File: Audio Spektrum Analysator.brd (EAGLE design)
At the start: 144.8 x 98.7 mm, 148 parts, among them IC1 LM324N, IC10 LM3914N, IC11 LM3914N, IC12 LM3914N, IC13 LM3914N, IC2 LM324N, IC3 LM324N, IC4 LM3914N, IC5 LM3914N, IC6 LM3914N, IC7 LM3914N, IC8 LM3914N, IC9 LM3914N, J2 DCJ0202, M1 ELECTRET_MICROPHON-F6050AP

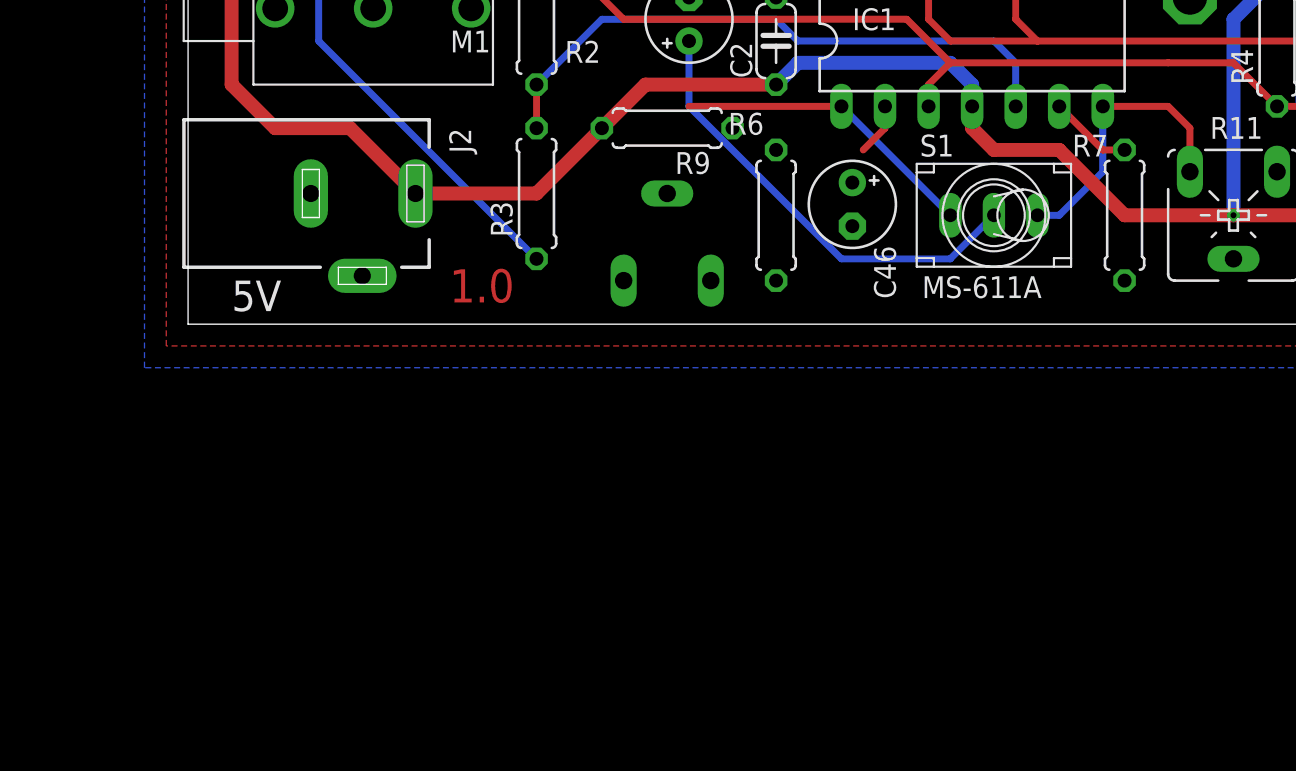
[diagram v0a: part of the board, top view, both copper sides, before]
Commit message: edited preamp
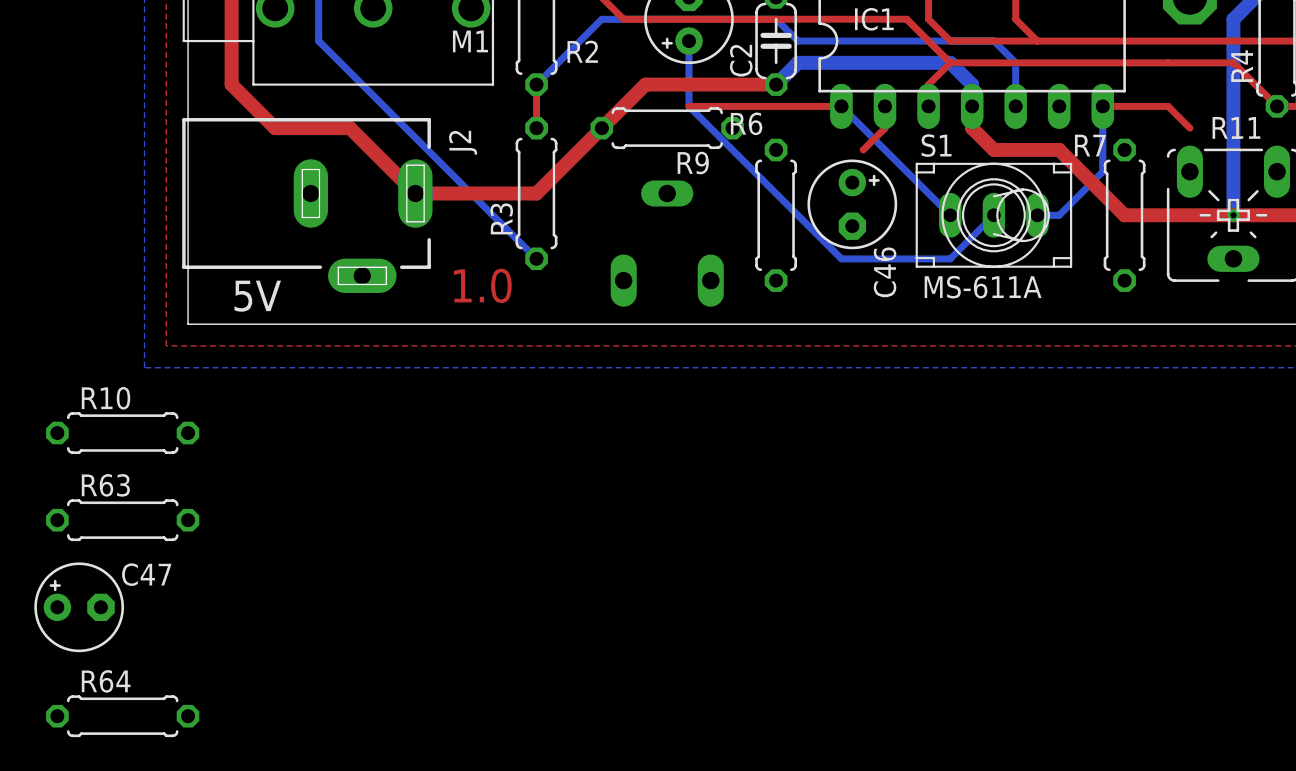
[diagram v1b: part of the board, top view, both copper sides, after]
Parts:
- added C47: 2u2, resistor:E2,5-5
- added R10, R63: 47k, rcl:0207/7
- added R64: 10k, rcl:0207/7
- R7: value 10k -> 100k
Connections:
- removed net N$123: IC1.6, R11.S, R7.2
- new net N$57: C47.+, IC1.6, R7.1
- new net N$70: C47.-, R64.2
- new net N$83: R11.E, R64.1
- net +5V: now also R63.2
- net GND: now also R10.1, R11.S; no longer R7.1
- net N$10: now also R7.2; no longer R11.E
- net N$3: now also R10.2, R63.1
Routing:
- net N$123: track 4.86 -> 0.00 mm
- net N$10: track 16.8 -> 14.3 mm

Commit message: edited reference circuit of LM3916s
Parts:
- removed R45: 1k2, resistor:0207/7
- removed R48, R50, R52, R54, R56, R58, R60, R62: 7k5, resistor:0207/7
- added R65: 1M, rcl:0207/7
- added R66, R67: 100k, rcl:0207/7
- added R68: 1k2, resistor:0207/7
- R43: value 1k2 -> 20k
- R44: value 7k5 -> 20k
- R46: value 7k5 -> 1k2
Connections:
- removed net N$107: IC4.6, IC4.7, R43.2
- removed net N$120: IC11.6, IC11.7, R57.2
- removed net N$121: IC11.8, R57.1, R58.2
- removed net N$127: IC12.6, IC12.7, R59.2
- removed net N$128: IC12.8, R59.1, R60.2
- removed net N$179: IC13.6, IC13.7, R61.2
- removed net N$180: IC13.8, R61.1, R62.2
- removed net N$82: IC10.8, R55.1, R56.2
- removed net N$94: IC9.6, IC9.7, R53.2
- removed net N$95: IC9.8, R53.1, R54.2
- new net RHI: IC10.6, IC11.6, IC12.6, IC13.6, IC4.6, IC5.6, IC6.6, IC7.6, IC8.6, IC9.6, R43.1, R44.2
- net +5V: now also R43.2
- net GND: now also IC10.8, IC11.8, IC12.8, IC13.8, IC4.8, IC5.8, IC6.8, IC7.8, IC8.8, IC9.8, R47.1, R49.1, R51.1, R53.1, R55.1, R57.1, R59.1, R61.1, R65.1, R66.1, R67.1, R68.1; no longer R48.1, R50.1, R52.1, R54.1, R56.1, R58.1, R60.1, R62.1
- net N$108: now also IC4.7, R68.2; no longer IC4.8, R43.1, R44.2
- net N$29: no longer IC6.6
- net N$30: now also IC5.7, R46.2; no longer IC6.8, R47.1, R48.2
- net N$42: now also IC7.7, R49.2; no longer IC5.6, IC5.7, R45.2
- net N$43: now also IC8.7, R51.2; no longer IC5.8, R45.1, R46.2
- net N$55: now also IC10.7, R55.2; no longer IC7.6, IC7.7, R49.2
- net N$56: now also IC9.7, R53.2; no longer IC7.8, R49.1, R50.2
- net N$68: now also IC11.7, R57.2; no longer IC8.6, IC8.7, R51.2
- net N$69: now also IC12.7, R59.2; no longer IC8.8, R51.1, R52.2
- net N$81: now also IC13.7, R61.2; no longer IC10.6, IC10.7, R55.2
- net OUT1: now also R66.2
- net OUT2: now also R67.2
- net VER: now also R65.2
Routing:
- net RHI: track 0.00 -> 39.9 mm
- net N$95: track 14.4 -> 0.00 mm
- net N$82: track 14.4 -> 0.00 mm
- net N$69: track 14.4 -> 0.00 mm
- net N$128: track 14.4 -> 0.00 mm
- net N$121: track 14.4 -> 0.00 mm
- net N$56: track 14.4 -> 0.00 mm
- net N$30: track 14.4 -> 0.00 mm
- net N$108: track 14.4 -> 0.00 mm
- net N$180: track 14.4 -> 0.00 mm
- net N$43: track 14.4 -> 0.00 mm
- net N$127: track 6.77 -> 0.00 mm
- net N$120: track 6.77 -> 0.00 mm
- net N$107: track 6.77 -> 0.00 mm
- net N$55: track 6.77 -> 0.00 mm
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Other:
- board text added: "DC IN"
- board text removed: "5V"

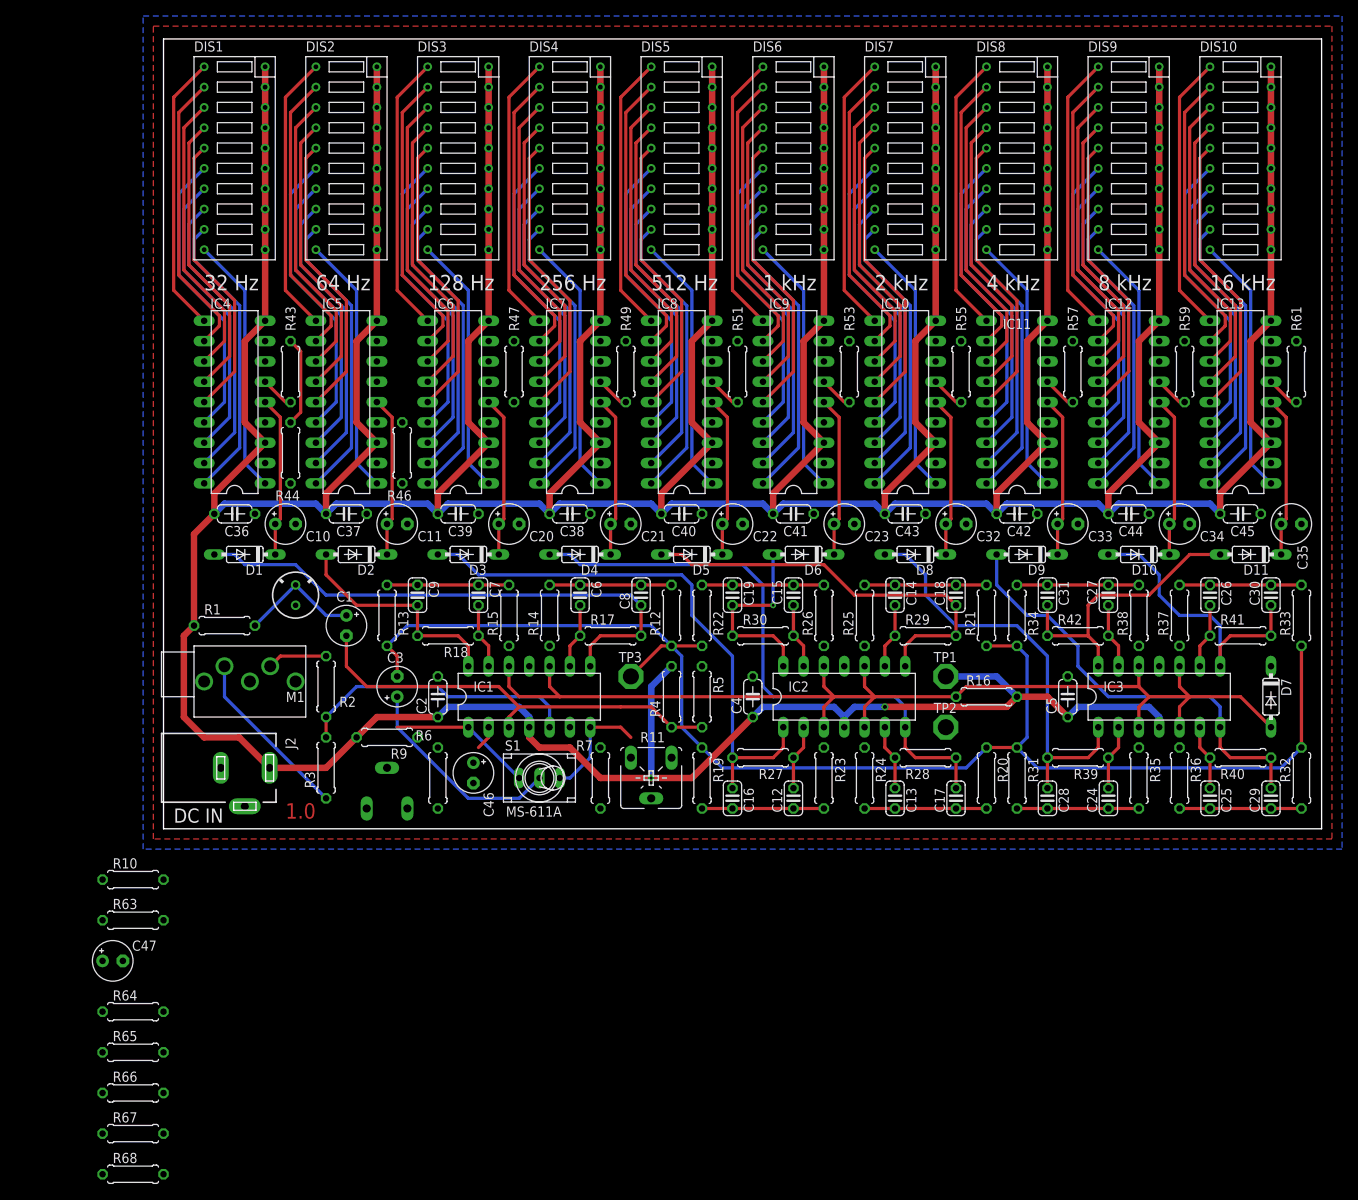
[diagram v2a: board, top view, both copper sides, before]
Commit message: started connecting Lm3916s
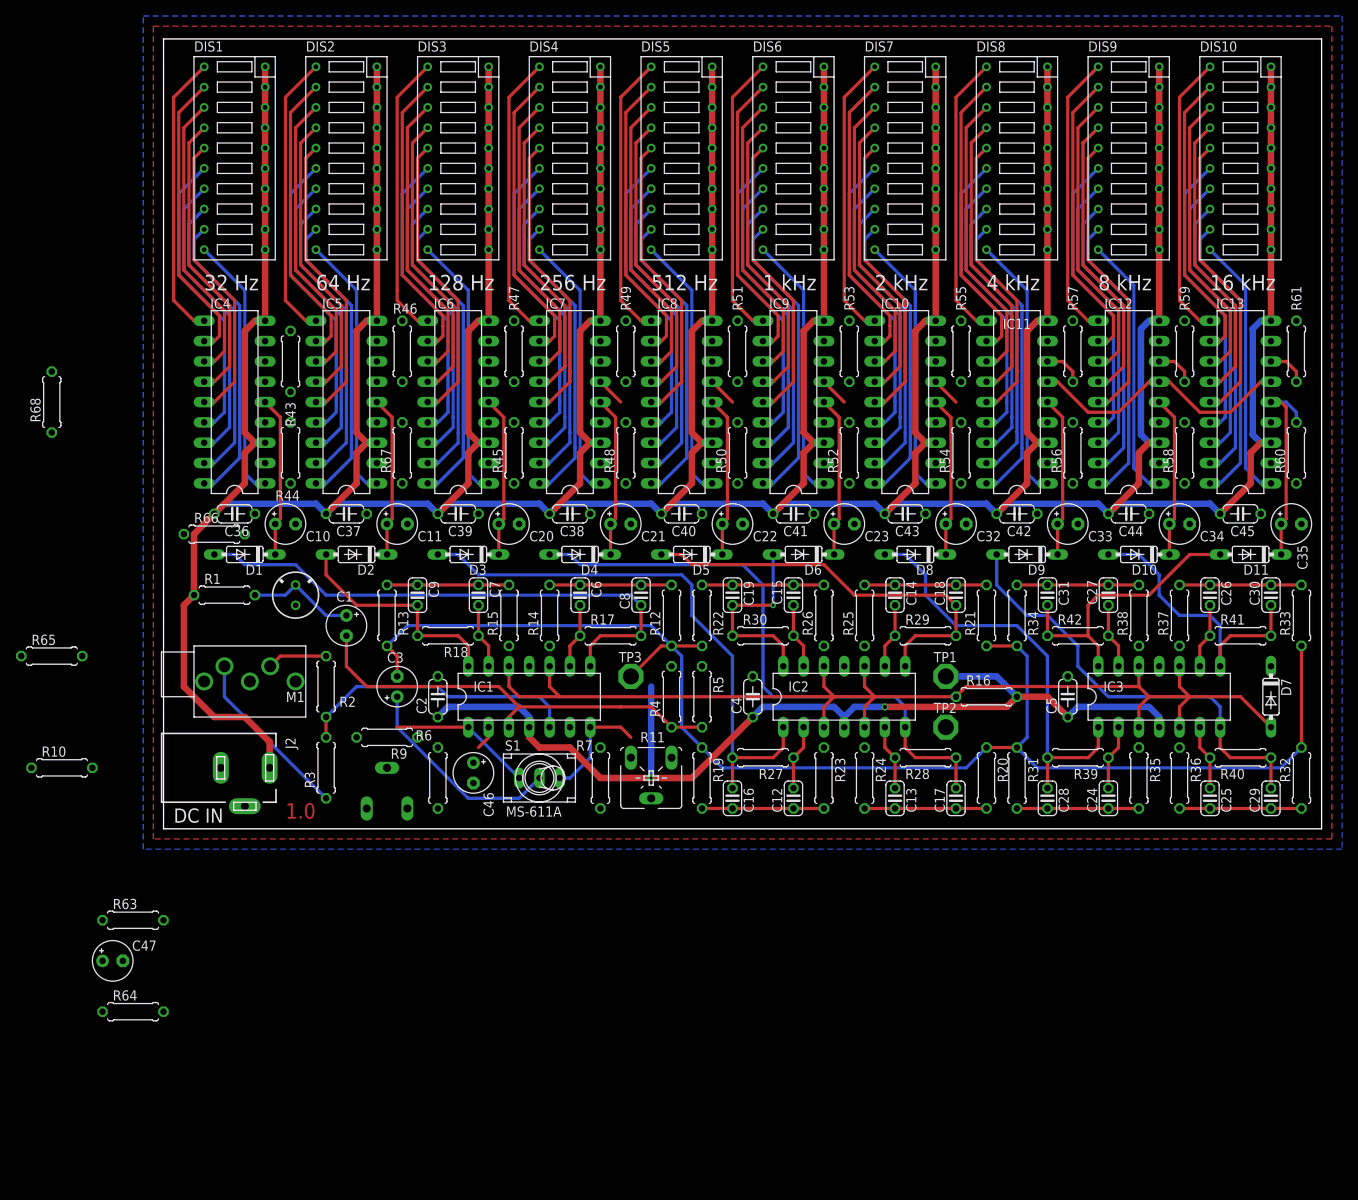
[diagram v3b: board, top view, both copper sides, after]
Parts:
- added R45, R48, R50, R52, R54, R56, R58, R60: 100k, rcl:0207/7
- moved R68 97.1 mm to (-14.0, 53.3), turned to 90 degrees
- moved R67 91.5 mm to (29.8, 47.0), turned to 90 degrees
- moved R66 70.6 mm to (6.35, 36.8)
- moved R65 50.6 mm to (-14.0, 21.6)
- moved R10 16.6 mm to (-12.7, 7.62)
- moved R46 12.7 mm to (29.8, 59.7), turned to 270 degrees
- moved R1 3.81 mm to (7.62, 29.2)
- moved R47 2.54 mm to (43.8, 59.7)
- moved R49 2.54 mm to (57.8, 59.7)
- moved R51 2.54 mm to (71.8, 59.7)
- moved R53 2.54 mm to (85.7, 59.7)
- moved R55 2.54 mm to (99.7, 59.7)
- moved R57 2.54 mm to (113.7, 59.7)
- moved R59 2.54 mm to (127.6, 59.7)
- moved R61 2.54 mm to (141.6, 59.7)
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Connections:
- net +5V renamed V+
- net GND: now also R45.1, R48.1, R50.1, R52.1, R54.1, R56.1, R58.1, R60.1
- net OUT10: now also R60.2
- net OUT3: now also R45.2
- net OUT4: now also R48.2
- net OUT5: now also R50.2
- net OUT6: now also R52.2
- net OUT7: now also R54.2
- net OUT8: now also R56.2
- net OUT9: now also R58.2
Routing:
- net V+: track 936.1 -> 920.2 mm
- net RHI: track 39.9 -> 48.6 mm
- net OUT10: track 20.1 -> 25.8 mm
- net N$69: track 0.00 -> 4.97 mm
- net N$68: track 0.00 -> 4.97 mm
- net N$81: track 0.00 -> 4.97 mm
- net N$13: track 15.1 -> 13.5 mm
- net N$58: track 36.5 -> 37.2 mm
- net N$174: track 36.0 -> 36.7 mm
- net N$100: track 36.5 -> 37.2 mm
- net N$99: track 36.5 -> 37.2 mm
- net N$97: track 36.5 -> 37.2 mm
- net N$93: track 34.9 -> 35.7 mm
- net N$92: track 36.0 -> 36.7 mm
- net N$90: track 36.0 -> 36.7 mm
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
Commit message: removed layers, further connected LM3916s
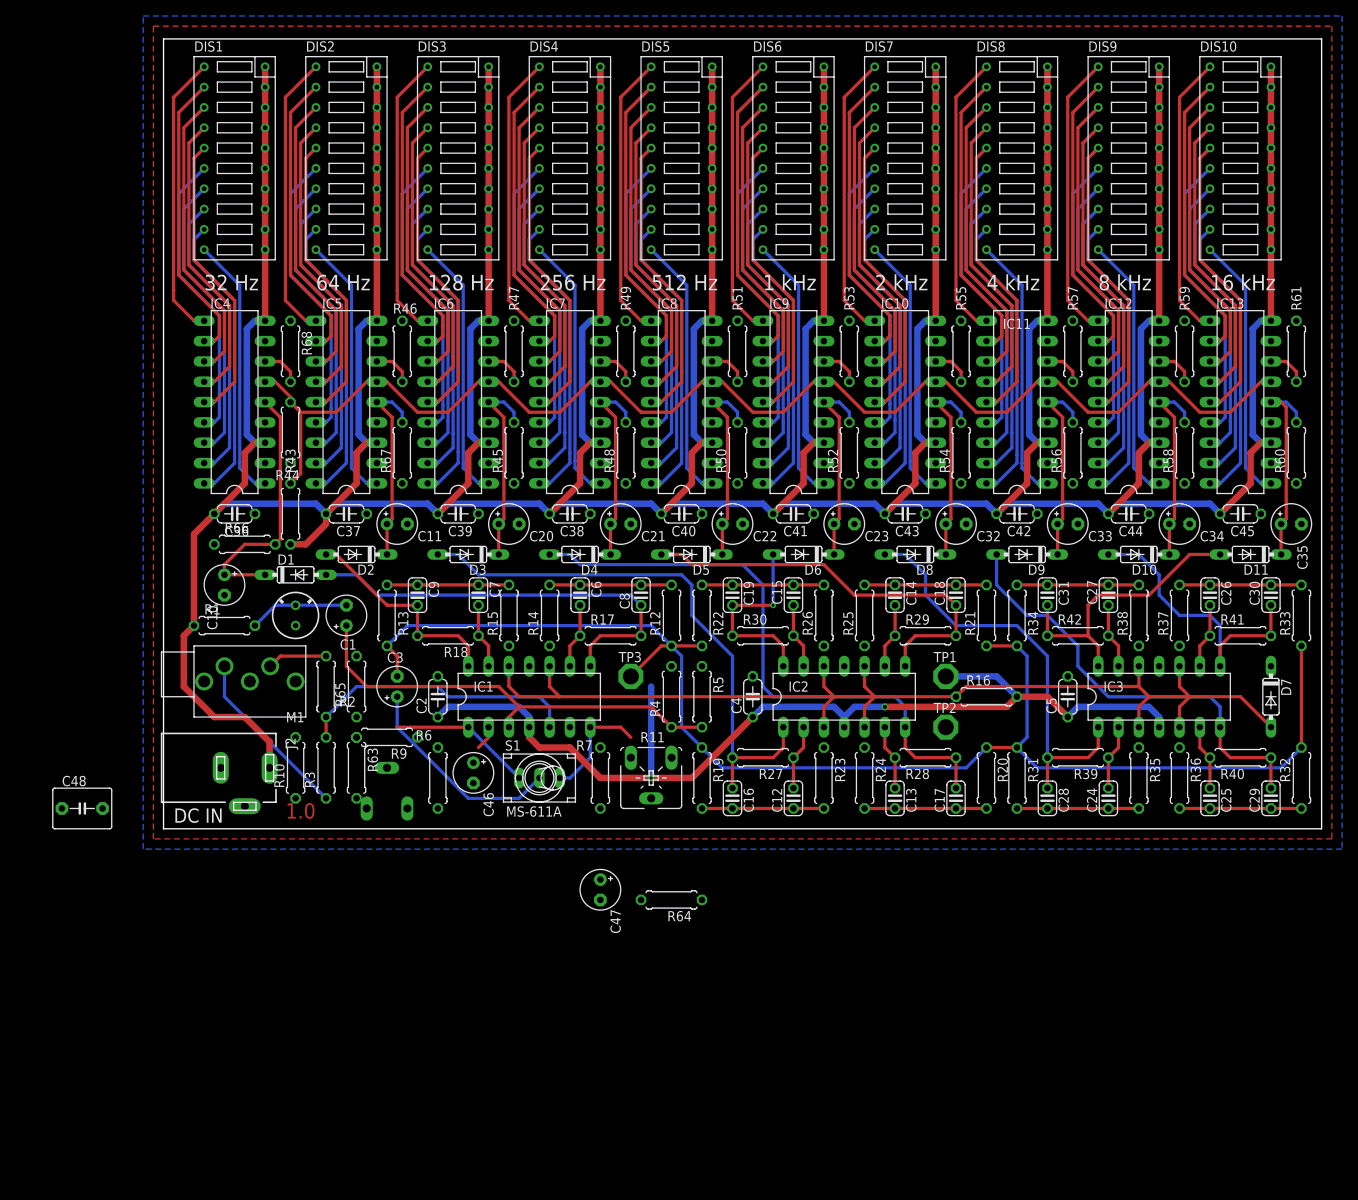
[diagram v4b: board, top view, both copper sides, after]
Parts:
- added C48: 1u, capacitor-wima:C5B5
- R11: value 10k -> 50k
- R64: value 10k -> 1k
- R7: value 100k -> 10k
- moved R64 68.7 mm to (63.5, -8.89), turned to 180 degrees
- moved C47 61.6 mm to (54.6, -7.62), turned to 270 degrees
- moved R65 38.3 mm to (24.1, 17.8), turned to 90 degrees
- moved R63 33.8 mm to (24.1, 7.62), turned to 270 degrees
- moved R68 30.5 mm to (15.9, 59.7), turned to 270 degrees
- moved R10 29.2 mm to (16.5, 7.62), turned to 90 degrees
- moved R43 19.1 mm to (15.9, 39.4), turned to 270 degrees
- moved C10 10.8 mm to (7.62, 30.5), turned to 270 degrees
- moved D1 6.84 mm to (16.5, 31.8), turned to 0 degrees
- moved R66 4.02 mm to (10.2, 35.6)
- moved R1 3.81 mm to (7.62, 25.4)
- moved M1 2.54 mm to (16.5, 26.7)
- moved R44 2.54 mm to (15.9, 49.5)
- moved C1 1.27 mm to (22.9, 26.7), turned to 90 degrees
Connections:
- net N$13: now also C1.-; no longer C1.+
- net N$4: now also C1.+; no longer C1.-
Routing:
- net RHI: track 48.6 -> 163.9 mm
- net V+: track 920.2 -> 935.5 mm
- net N$133: track 69.2 -> 54.2 mm
- net OUT1: track 20.1 -> 32.6 mm
- net OUT9: track 20.1 -> 25.1 mm
- net OUT8: track 20.1 -> 25.1 mm
- net OUT7: track 20.1 -> 25.1 mm
- net OUT6: track 20.1 -> 25.1 mm
- net OUT5: track 20.1 -> 25.1 mm
- net OUT4: track 20.1 -> 25.1 mm
- net OUT3: track 20.1 -> 25.1 mm
- net OUT2: track 20.1 -> 25.1 mm
- net N$108: track 0.00 -> 4.97 mm
- net N$56: track 0.00 -> 4.97 mm
- net N$55: track 0.00 -> 4.97 mm
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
